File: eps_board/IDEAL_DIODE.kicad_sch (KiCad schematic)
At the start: 7 parts, among them U20 TPS2115ADRBR

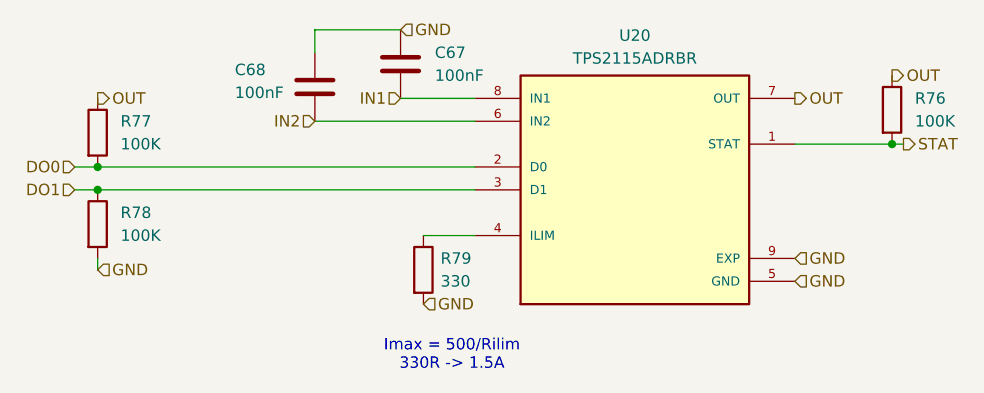
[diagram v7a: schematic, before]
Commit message: use small connectors in corners and on sides for sun sensors and solar cells
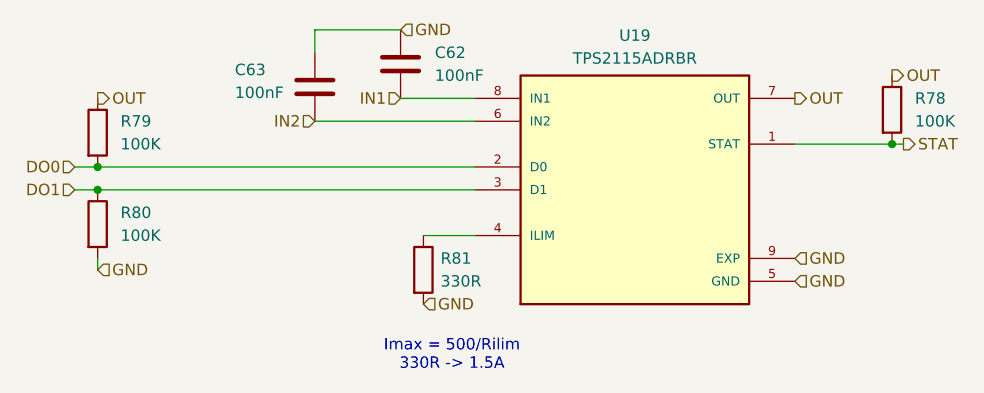
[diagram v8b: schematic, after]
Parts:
- R81: renamed from R79; value 330 -> 330R
- renumbered C67 to C62, C68 to C63, R76 to R78, R77 to R79, R78 to R80, U20 to U19
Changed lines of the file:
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@@
 		(dnp no)
 		(fields_autoplaced yes)
-		(property "Reference" "R79"
+		(property "Reference" "R81"
 			(at 115.57 98.4249 0)
 			(effects
@@
 			)
 		)
-		(property "Value" "330"
+		(property "Value" "330R"
 			(at 115.57 100.9649 0)
 			(effects
@@
 		)
 		(property "Tolerance" "1"
+			(at 113.665 99.695 0)
+			(effects
+				(font
+					(size 1.27 1.27)
+				)
+				(hide yes)
+			)
+		)
+		(property "Manufactorer" ""
 			(at 113.665 99.695 0)
 			(effects
@@
 			(project "EPS"
 				(path "/05170af6-30ef-4c3a-b972-f098085da1bc/00000000-0000-0000-0000-00005f71f783"
-					(reference "R79")
+					(reference "R81")
 					(unit 1)
 				)
@@
 		(dnp no)
 		(fields_autoplaced yes)
-		(property "Reference" "R77"
+		(property "Reference" "R79"
 			(at 80.01 83.1849 0)
 			(effects
@@
 		)
 		(property "Tolerance" "1"
+			(at 77.47 84.455 0)
+			(effects
+				(font
+					(size 1.27 1.27)
+				)
+				(hide yes)
+			)
+		)
+		(property "Manufactorer" ""
 			(at 77.47 84.455 0)
 			(effects
@@
 			(project "EPS"
 				(path "/05170af6-30ef-4c3a-b972-f098085da1bc/00000000-0000-0000-0000-00005f71f783"
-					(reference "R77")
+					(reference "R79")
 					(unit 1)
 				)
@@
 		(dnp no)
 		(fields_autoplaced yes)
-		(property "Reference" "R76"
+		(property "Reference" "R78"
 			(at 168.275 80.6449 0)
 			(effects
@@
 		)
 		(property "Tolerance" "1"
+			(at 165.735 81.915 0)
+			(effects
+				(font
+					(size 1.27 1.27)
+				)
+				(hide yes)
+			)
+		)
+		(property "Manufactorer" ""
 			(at 165.735 81.915 0)
 			(effects
@@
 			(project "EPS"
 				(path "/05170af6-30ef-4c3a-b972-f098085da1bc/00000000-0000-0000-0000-00005f71f783"
-					(reference "R76")
+					(reference "R78")
 					(unit 1)
 				)
@@
 		(dnp no)
 		(fields_autoplaced yes)
-		(property "Reference" "U20"
+		(property "Reference" "U19"
 			(at 137.16 73.66 0)
 			(effects
@@
 		)
 		(property "Part Number" "TPS2115ADRBR "
+			(at 137.16 90.805 0)
+			(effects
+				(font
+					(size 1.27 1.27)
+				)
+				(hide yes)
+			)
+		)
+		(property "Manufactorer" ""
 			(at 137.16 90.805 0)
 			(effects
@@
 			(project ""
 				(path "/05170af6-30ef-4c3a-b972-f098085da1bc/00000000-0000-0000-0000-00005f71f783"
-					(reference "U20")
+					(reference "U19")
 					(unit 1)
 				)
@@
 		(dnp no)
 		(fields_autoplaced yes)
-		(property "Reference" "C67"
+		(property "Reference" "C62"
 			(at 114.935 75.5649 0)
 			(effects
@@
 		)
 		(property "Tolerance" "10"
+			(at 111.125 76.835 0)
+			(effects
+				(font
+					(size 1.27 1.27)
+				)
+				(hide yes)
+			)
+		)
+		(property "Manufactorer" ""
 			(at 111.125 76.835 0)
 			(effects
@@
 			(project ""
 				(path "/05170af6-30ef-4c3a-b972-f098085da1bc/00000000-0000-0000-0000-00005f71f783"
-					(reference "C67")
+					(reference "C62")
 					(unit 1)
 				)
@@
 		(dnp no)
 		(fields_autoplaced yes)
-		(property "Reference" "R78"
+		(property "Reference" "R80"
 			(at 80.01 93.3449 0)
 			(effects
@@
 		)
 		(property "Tolerance" "1"
+			(at 77.47 94.615 0)
+			(effects
+				(font
+					(size 1.27 1.27)
+				)
+				(hide yes)
+			)
+		)
+		(property "Manufactorer" ""
 			(at 77.47 94.615 0)
 			(effects
@@
 			(project ""
 				(path "/05170af6-30ef-4c3a-b972-f098085da1bc/00000000-0000-0000-0000-00005f71f783"
-					(reference "R78")
+					(reference "R80")
 					(unit 1)
 				)
@@
 		(on_board yes)
 		(dnp no)
-		(property "Reference" "C68"
+		(property "Reference" "C63"
 			(at 92.71 77.47 0)
 			(effects
@@
 		)
 		(property "Tolerance" "10"
+			(at 101.6 79.375 0)
+			(effects
+				(font
+					(size 1.27 1.27)
+				)
+				(hide yes)
+			)
+		)
+		(property "Manufactorer" ""
 			(at 101.6 79.375 0)
 			(effects
@@
 			(project "EPS"
 				(path "/05170af6-30ef-4c3a-b972-f098085da1bc/00000000-0000-0000-0000-00005f71f783"
-					(reference "C68")
+					(reference "C63")
 					(unit 1)
 				)
